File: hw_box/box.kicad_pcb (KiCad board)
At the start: 2 copper layers, 46.2 x 49.1 mm, 32 parts, among them J1 Conn_2Rows-05Pins, SW1 SW_DPST_x2, T1 Tab, U1 PY32F002AF15P6TU

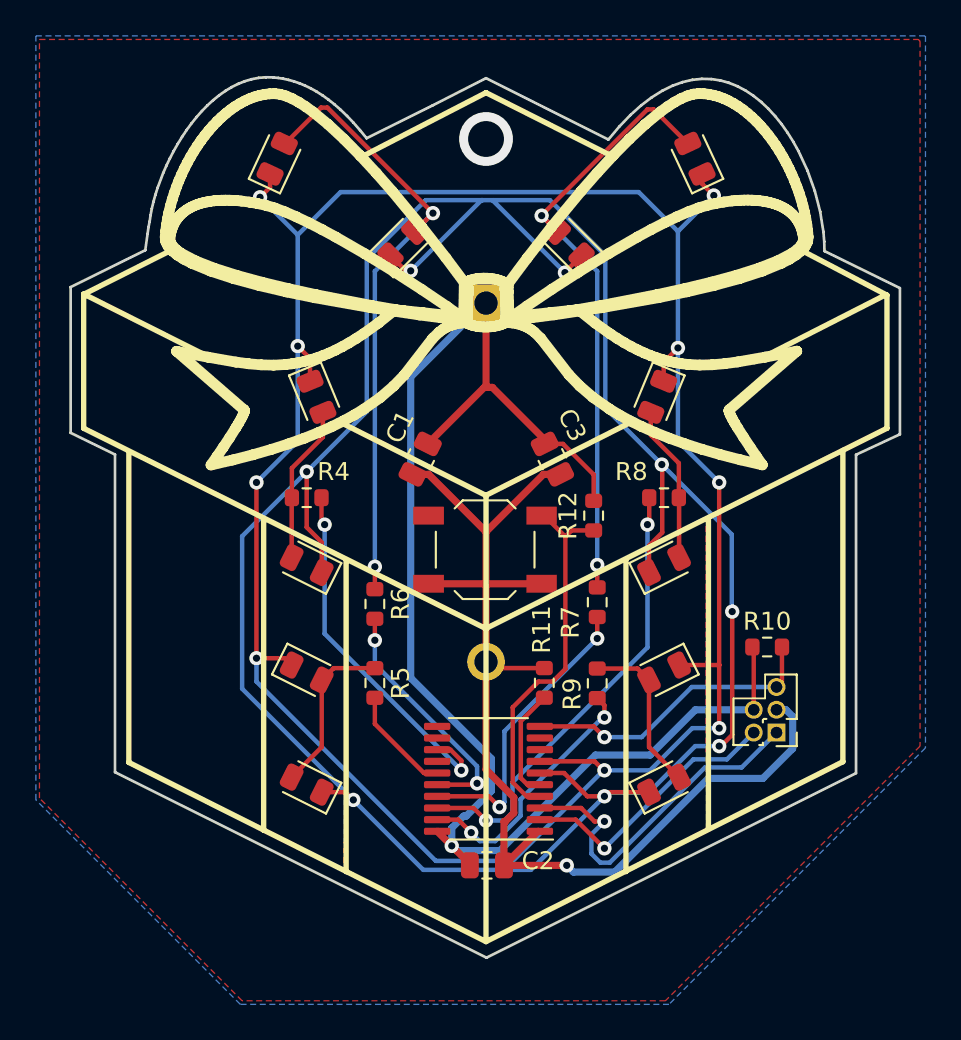
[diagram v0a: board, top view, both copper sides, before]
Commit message: box Rev.B
modified the F. Mask, and rotate the Led4 and Led12
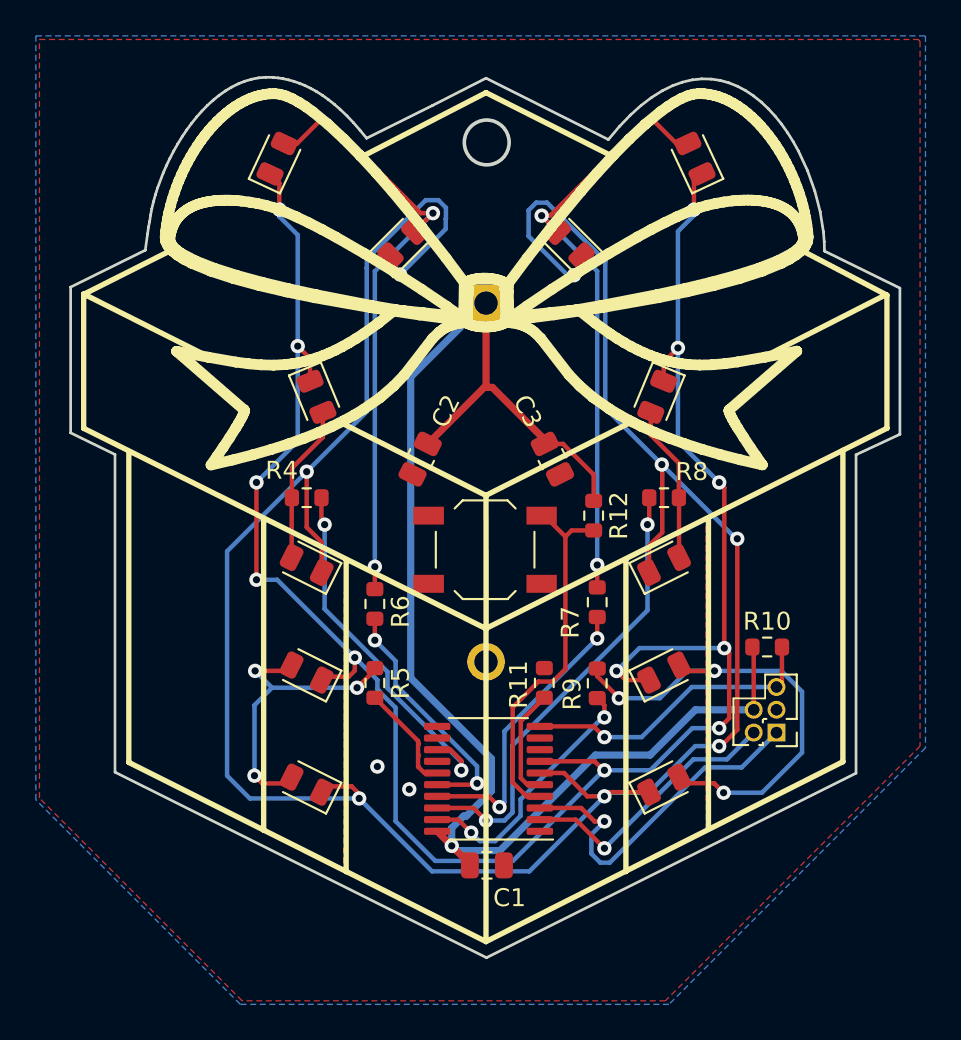
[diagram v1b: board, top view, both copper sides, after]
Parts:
- moved C1 23.0 mm to (175.1, 88.5), turned to 180 degrees
- moved C2 23.0 mm to (171.3, 65.8), turned to -116.566 degrees
- turned D12 to 26.566 degrees
- turned D4 to 153.436 degrees
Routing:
- net GND: track 64.9 -> 0.07 mm
- net Net-(D12-A): track 9.26 -> 27.1 mm, vias 0 -> 3
- net /MPX2: track 132.0 -> 116.0 mm, vias 9 -> 12
- net Net-(D4-A): track 9.34 -> 17.4 mm, vias 0 -> 3
- net /MPX1: track 142.2 -> 140.9 mm
- net Net-(D6-A): track 35.3 -> 34.8 mm
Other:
- outline, holes or cut-outs redrawn
- board text added: "Rev. B"
- board text removed: "Rev. A"
